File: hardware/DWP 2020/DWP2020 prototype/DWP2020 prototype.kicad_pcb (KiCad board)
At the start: 2 copper layers, 2 parts, among them U1 Teensy4.0, U2 SSD1351_128X128_LCD-bGeigieNa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

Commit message: fix some typoos
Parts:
- U2: value SSD1351_128X128_LCD-bGeigieNanoKit_V1.1r5a-eagle-import -> SSD1351_128X128
- moved U2 13.7 mm to (1008.4, 35.6)
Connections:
- U2 pad JP1$7: Net-(U2-PadJP1$7) -> Net-(U1-Pad33)
- U2 pad JP1$8: Net-(U2-PadJP1$8) -> Net-(U1-Pad1)
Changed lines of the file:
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@@
-(kicad_pcb (version 20200614) (host pcbnew "5.99.0-unknown-0bfe413~88~ubuntu18.04.1")
+(kicad_pcb (version 20200614) (host pcbnew "5.99.0-unknown-0dd34d1~88~ubuntu18.04.1")
   (general
     (thickness 1.6)
@@
     (tracks 0)
     (modules 2)
-    (nets 56)
+    (nets 54)
   )
   (paper "A4")
@@
   (net 49 "Net-(U2-PadJP1$5)")
   (net 50 "Net-(U2-PadJP1$6)")
-  (net 51 "Net-(U2-PadJP1$7)")
-  (net 52 "Net-(U2-PadJP1$8)")
-  (net 53 "Net-(U2-PadJP1$9)")
-  (net 54 "Net-(U2-PadJP1$10)")
-  (net 55 "Net-(U2-PadJP1$11)")
+  (net 51 "Net-(U2-PadJP1$9)")
+  (net 52 "Net-(U2-PadJP1$10)")
+  (net 53 "Net-(U2-PadJP1$11)")
   (net_class "Default" "This is the default net class."
     (clearance 0.2)
@@
     (add_net "Net-(U2-PadJP1$5)")
     (add_net "Net-(U2-PadJP1$6)")
-    (add_net "Net-(U2-PadJP1$7)")
-    (add_net "Net-(U2-PadJP1$8)")
     (add_net "Net-(U2-PadJP1$9)")
   )
   (module "DWP2020 prototype:SSD1351_128X128_LCD" (layer "F.Cu")
-    (at 1013.46 22.86)
+    (at 1008.38 35.56)
     (fp_text reference "U2" (at 6.35 20.32) (layer "F.SilkS")
       (effects (font (size 1.6891 1.6891) (thickness 0.135128)) (justify left bottom))
     )
-    (fp_text value "SSD1351_128X128_LCD-bGeigieNanoKit_V1.1r5a-eagle-import" (at 0 0) (layer "F.SilkS") hide
+    (fp_text value "SSD1351_128X128" (at 0 0) (layer "F.SilkS") hide
       (effects (font (size 1.27 1.27) (thickness 0.15)))
     )
@@
       (net 50 "Net-(U2-PadJP1$6)") (pinfunction "3.3V") (solder_mask_margin 0.1016))
     (pad "JP1$7" thru_hole circle (at 11.78499 -17.190009 90) (size 1.778 1.778) (drill 1) (layers *.Cu *.Mask)
-      (net 51 "Net-(U2-PadJP1$7)") (pinfunction "VDD") (solder_mask_margin 0.1016))
+      (net 25 "Net-(U1-Pad33)") (pinfunction "VDD") (solder_mask_margin 0.1016))
     (pad "JP1$8" thru_hole circle (at 14.32499 -17.190009 90) (size 1.778 1.778) (drill 1) (layers *.Cu *.Mask)
-      (net 52 "Net-(U2-PadJP1$8)") (pinfunction "GND") (solder_mask_margin 0.1016))
+      (net 11 "Net-(U1-Pad1)") (pinfunction "GND") (solder_mask_margin 0.1016))
     (pad "U$23$P$1" thru_hole circle (at 19.300012 -17.260012) (size 3.2 3.2) (drill 2.5) (layers *.Cu *.Mask)
       (solder_mask_margin 0.1016))
@@
       (solder_mask_margin 0.1016))
     (pad "JP1$9" thru_hole circle (at -11.075009 -17.190009 90) (size 1.778 1.778) (drill 1) (layers *.Cu *.Mask)
-      (net 53 "Net-(U2-PadJP1$9)") (pinfunction "SI") (solder_mask_margin 0.1016))
+      (net 51 "Net-(U2-PadJP1$9)") (pinfunction "SI") (solder_mask_margin 0.1016))
     (pad "JP1$10" thru_hole circle (at -8.535009 -17.190009 90) (size 1.778 1.778) (drill 1) (layers *.Cu *.Mask)
-      (net 54 "Net-(U2-PadJP1$10)") (pinfunction "CL") (solder_mask_margin 0.1016))
+      (net 52 "Net-(U2-PadJP1$10)") (pinfunction "CL") (solder_mask_margin 0.1016))
     (pad "JP1$11" thru_hole circle (at -5.995009 -17.190009 90) (size 1.778 1.778) (drill 1) (layers *.Cu *.Mask)
-      (net 55 "Net-(U2-PadJP1$11)") (pinfunction "DC") (solder_mask_margin 0.1016))
+      (net 53 "Net-(U2-PadJP1$11)") (pinfunction "DC") (solder_mask_margin 0.1016))
   )
   (module "Teensy:Teensy40" (layer "F.Cu")

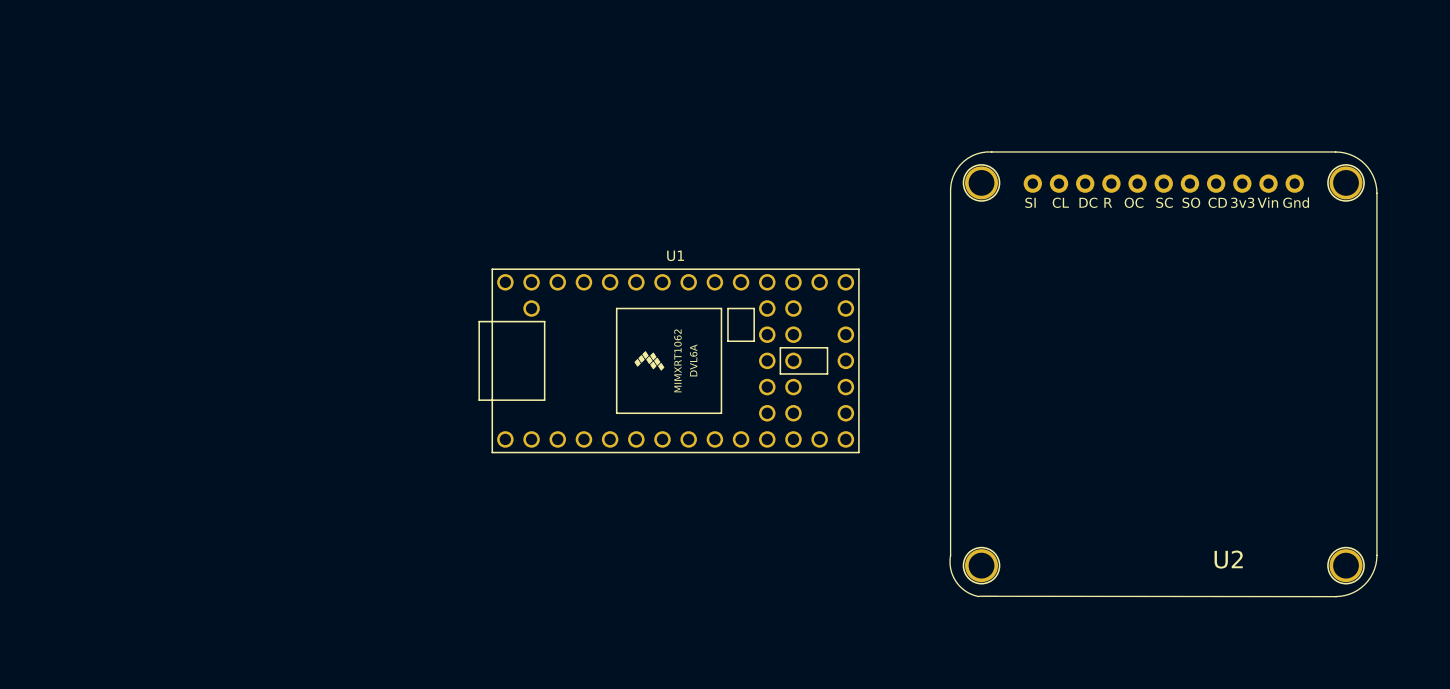
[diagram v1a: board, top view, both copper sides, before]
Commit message: Updated ProtoType drawings
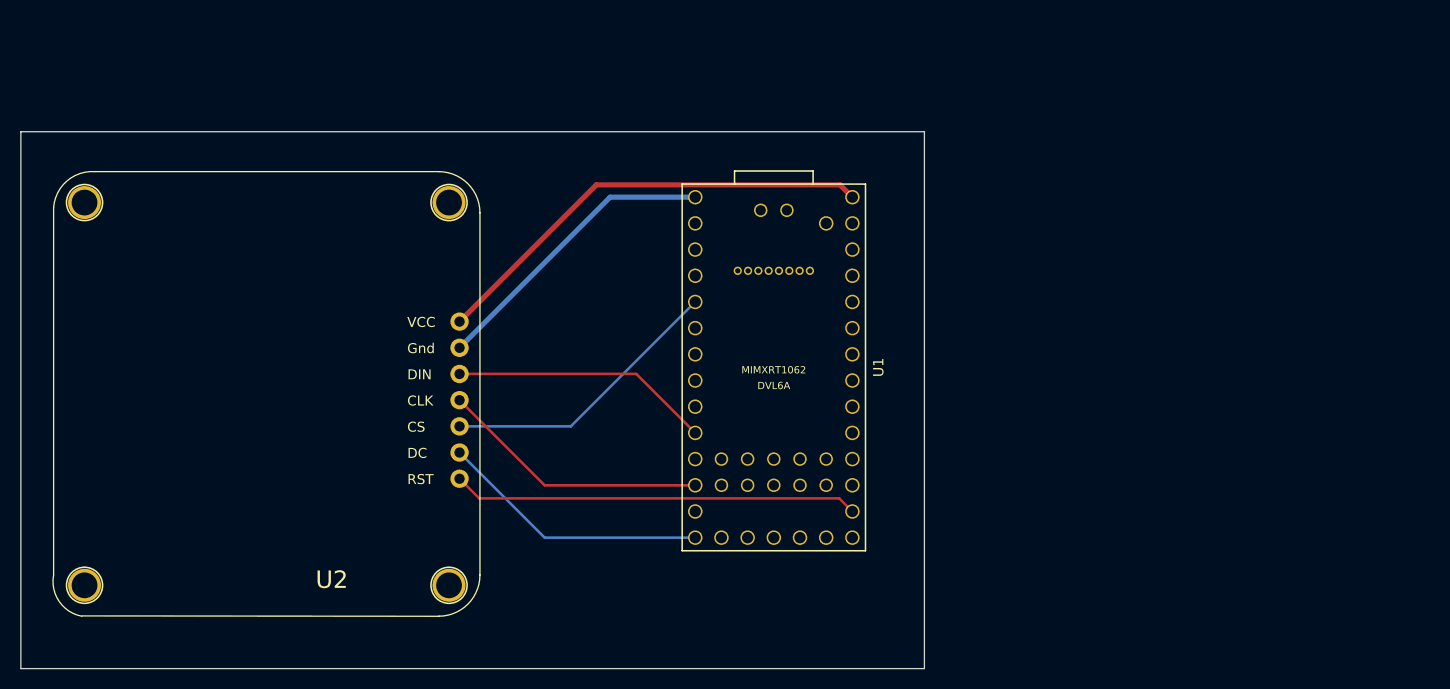
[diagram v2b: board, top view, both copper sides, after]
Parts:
- U1: footprint Teensy:Teensy40 -> Teensy:Teensy40_SMT
- U2: value SSD1351_128X128 -> SSD1351_128X128_Waveshare; footprint DWP2020 prototype:SSD1351_128X128_LCD -> DWP2020 prototype:SSD1351_128X128_LCD Waveshare
- moved U2 87.0 mm to (921.4, 37.5)
- moved U1 9.55 mm to (972.2, 36.2), turned to -90 degrees
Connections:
- U2 pad JP1$1: Net-(U2-PadJP1$1) -> Net-(U1-Pad33)
- U2 pad JP1$2: Net-(U2-PadJP1$2) -> Net-(U1-Pad1)
- U2 pad JP1$3: Net-(U2-PadJP1$3) -> Net-(U1-Pad10)
- U2 pad JP1$4: Net-(U2-PadJP1$4) -> Net-(U1-Pad12)
- U2 pad JP1$5: Net-(U2-PadJP1$5) -> Net-(U1-Pad5)
- U2 pad JP1$6: Net-(U2-PadJP1$6) -> Net-(U1-Pad14)
- U2 pad JP1$7: Net-(U1-Pad33) -> Net-(U1-Pad21)
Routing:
- net Net-(U1-Pad33): track 0.00 -> 44.1 mm
- net Net-(U1-Pad21): track 0.00 -> 39.4 mm
- net Net-(U1-Pad1): track 0.00 -> 28.9 mm
- net Net-(U1-Pad5): track 0.00 -> 27.9 mm
- net Net-(U1-Pad12): track 0.00 -> 26.3 mm
- net Net-(U1-Pad14): track 0.00 -> 26.3 mm
- net Net-(U1-Pad10): track 0.00 -> 25.2 mm
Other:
- board outline added: 87.6 x 52.1 mm
- net class Power added: clearance 0.2, trace_width 0.5, via_dia 0.8, via_drill 0.4

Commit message: Updated schemtics and board
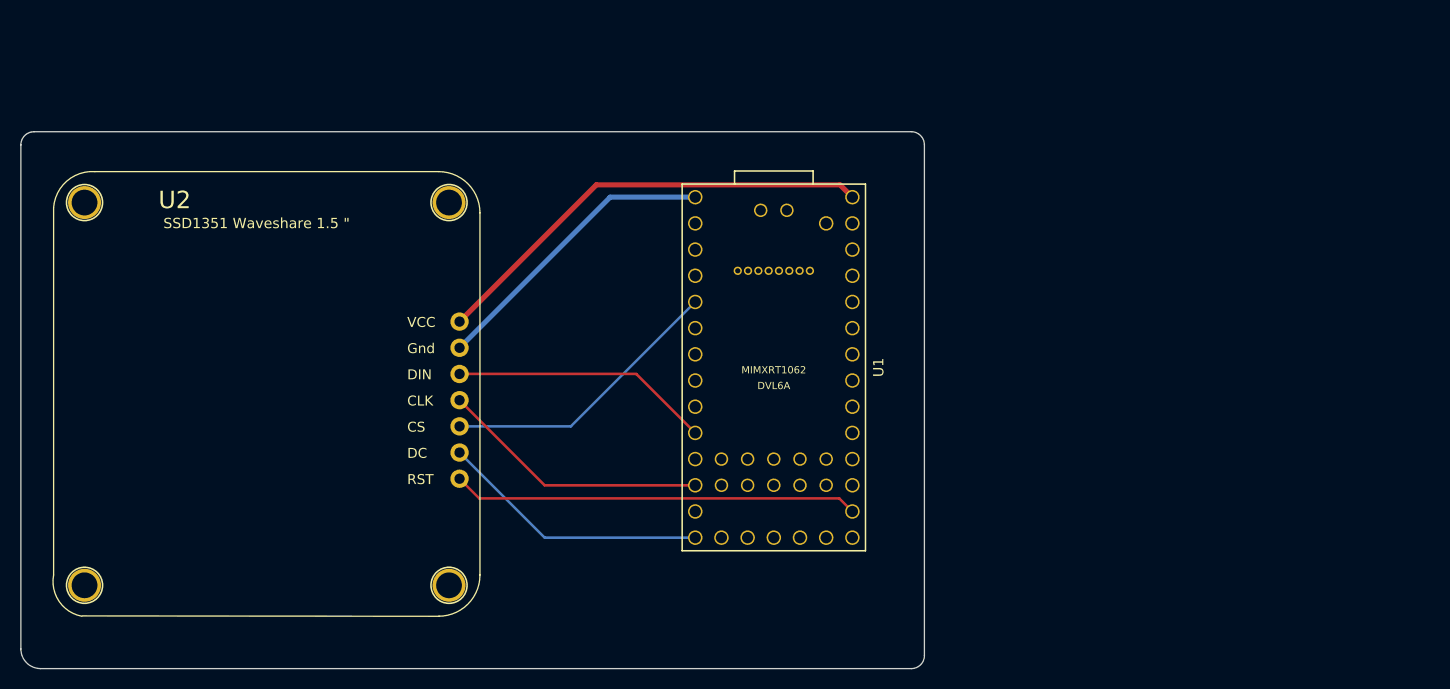
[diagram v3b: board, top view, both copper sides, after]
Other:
- outline, holes or cut-outs redrawn
- board text added: "SSD1351 Waveshare 1.5 ""
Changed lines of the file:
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@@
-(kicad_pcb (version 20200614) (host pcbnew "5.99.0-unknown-aa7ce74~88~ubuntu18.04.1")
+(kicad_pcb (version 20200614) (host pcbnew "5.99.0-unknown-09cb75b~88~ubuntu18.04.1")
   (general
     (thickness 1.6)
-    (drawings 4)
+    (drawings 9)
     (tracks 16)
     (modules 2)
@@
   (module "DWP2020 prototype:SSD1351_128X128_LCD Waveshare" (layer "F.Cu")
     (at 921.385 37.465)
-    (fp_text reference "U2" (at 6.35 20.32) (layer "F.SilkS")
+    (fp_text reference "U2" (at -8.89 -16.51) (layer "F.SilkS")
       (effects (font (size 1.6891 1.6891) (thickness 0.135128)) (justify left bottom))
     )
@@
       (net 43 "Net-(U1-Pad21)") (pinfunction "RST") (solder_mask_margin 0.1016))
   )
-  (gr_line (start 899.16 65.405) (end 899.16 13.335) (layer "Edge.Cuts") (width 0.05))
-  (gr_line (start 986.79 65.405) (end 899.16 65.405) (layer "Edge.Cuts") (width 0.05))
-  (gr_line (start 986.79 13.335) (end 986.79 65.405) (layer "Edge.Cuts") (width 0.05))
-  (gr_line (start 899.16 13.335) (end 986.79 13.335) (layer "Edge.Cuts") (width 0.05))
+  (gr_text "SSD1351 Waveshare 1.5 \"" (at 922.02 22.225) (layer "F.SilkS")
+    (effects (font (size 1 1) (thickness 0.15)))
+  )
+  (gr_arc (start 985.52 14.605) (end 986.79 14.605) (angle -90) (layer "Edge.Cuts") (width 0.05))
+  (gr_arc (start 985.52 64.135) (end 985.52 65.405) (angle -90) (layer "Edge.Cuts") (width 0.05))
+  (gr_arc (start 901.065 63.5) (end 899.16 63.5) (angle -90) (layer "Edge.Cuts") (width 0.05))
+  (gr_arc (start 900.43 14.605) (end 900.43 13.335) (angle -90) (layer "Edge.Cuts") (width 0.05))
+  (gr_line (start 899.16 63.5) (end 899.16 14.605) (layer "Edge.Cuts") (width 0.05))
+  (gr_line (start 985.52 65.405) (end 901.065 65.405) (layer "Edge.Cuts") (width 0.05))
+  (gr_line (start 986.79 14.605) (end 986.79 64.135) (layer "Edge.Cuts") (width 0.05))
+  (gr_line (start 900.43 13.335) (end 985.52 13.335) (layer "Edge.Cuts") (width 0.05))
   (segment (start 949.96 52.705) (end 964.565 52.705) (width 0.25) (layer "B.Cu") (net 44))
   (segment (start 941.705 44.45) (end 949.96 52.705) (width 0.25) (layer "B.Cu") (net 44))
